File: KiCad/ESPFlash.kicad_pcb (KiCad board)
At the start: 2 copper layers, 29.8 x 23 mm, 26 parts, among them J1 USB-C-16P (USB 2.0 only), J2 ESPFlash, Q1 MMDT3904, U1 TLV75533PDBVR, U2 USBLC6-4SC6, U3 CP2102N-Axx-xQFN24

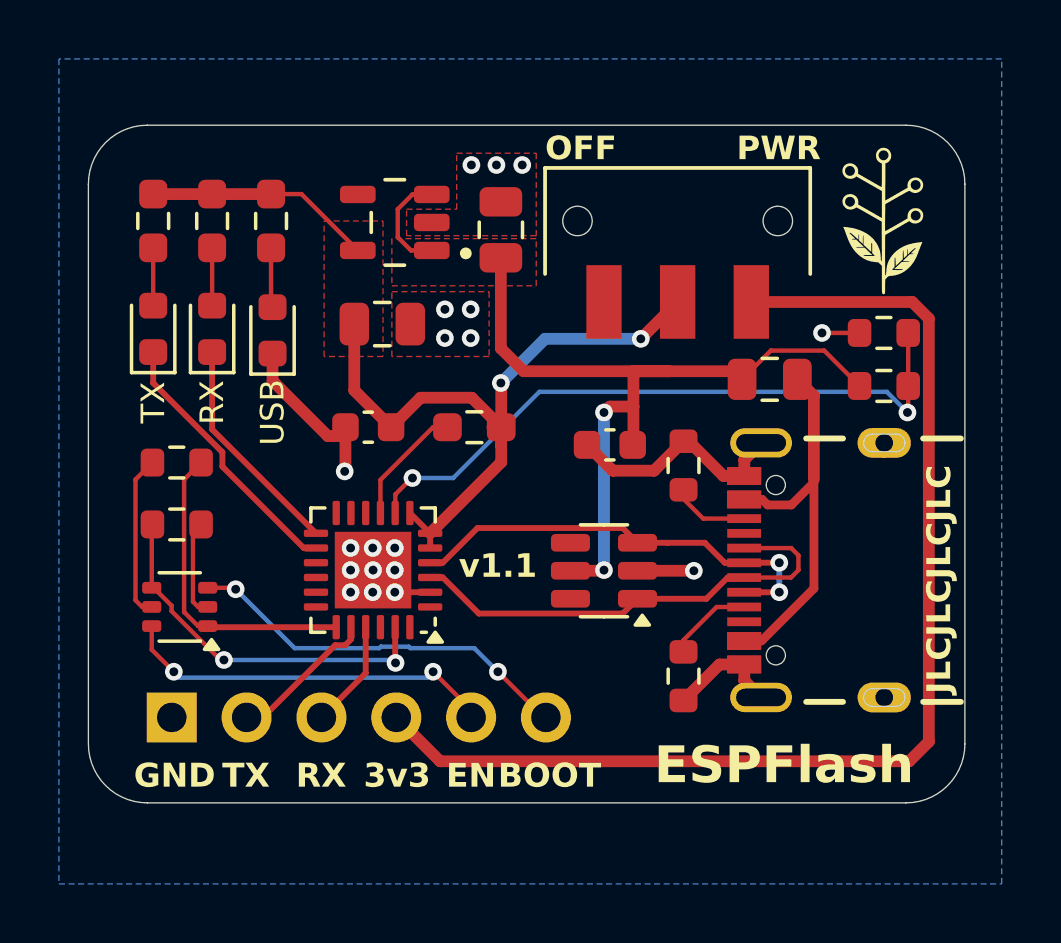
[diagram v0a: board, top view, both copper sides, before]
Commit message: Update BoM
Update components with full description and Digikey P/N.
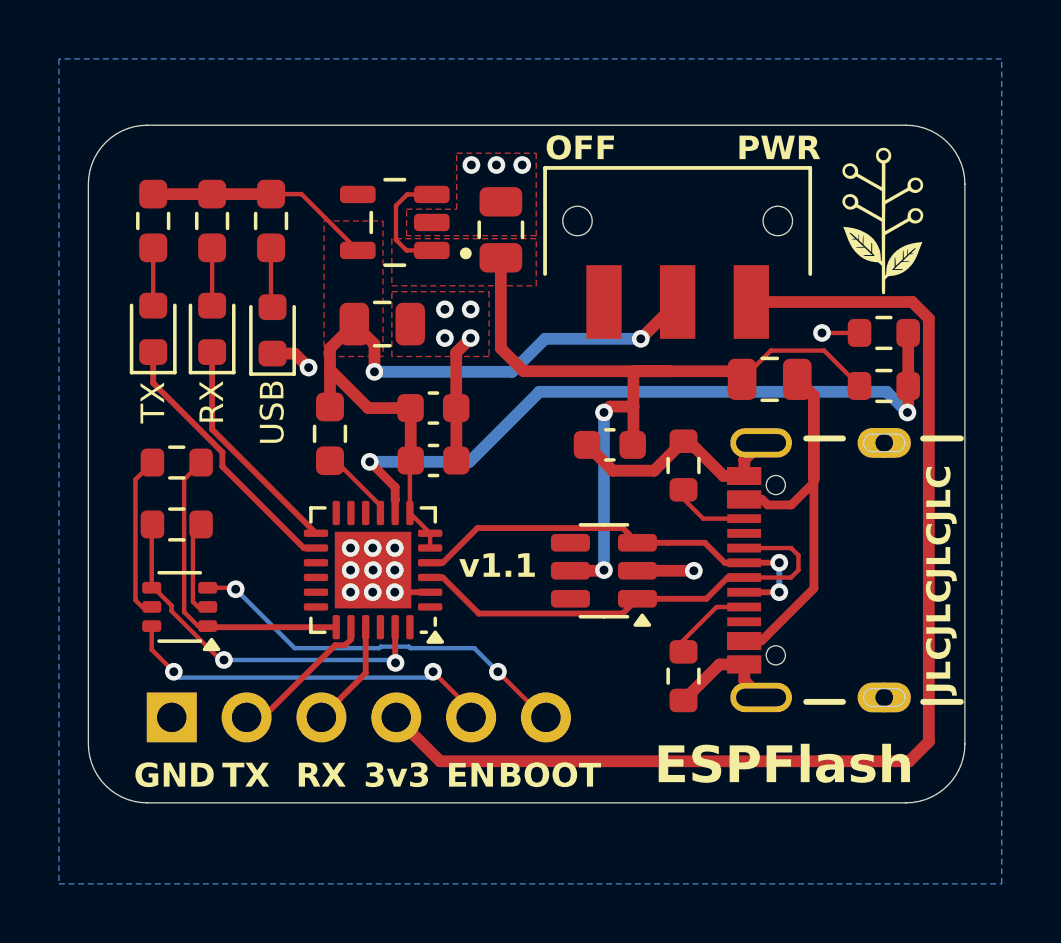
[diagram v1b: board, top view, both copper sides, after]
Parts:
- added C4: 4.7u, Capacitor_SMD:C_0603_1608Metric, F.Cu at (48.7, 30.9)
- moved R4 4.91 mm to (45.2, 31.7), turned to 90 degrees
- moved C5 2.49 mm to (48.7, 32.6), turned to 0 degrees
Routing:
- net Net-(U3-~{RST}): track 4.14 -> 2.60 mm
- net Net-(U3-VBUS): track 22.4 -> 23.9 mm
- net +3.3V: track 31.4 -> 32.6 mm
- net GND: track 21.8 -> 22.6 mm

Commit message: Update BOM and general tidy-up
Include DigiKey cut-tape components and add flag to indicate own stocked items. Remove files that aren't part of the sharable project (KiCad 9 embeds), Remove empty/irrelevant folders.
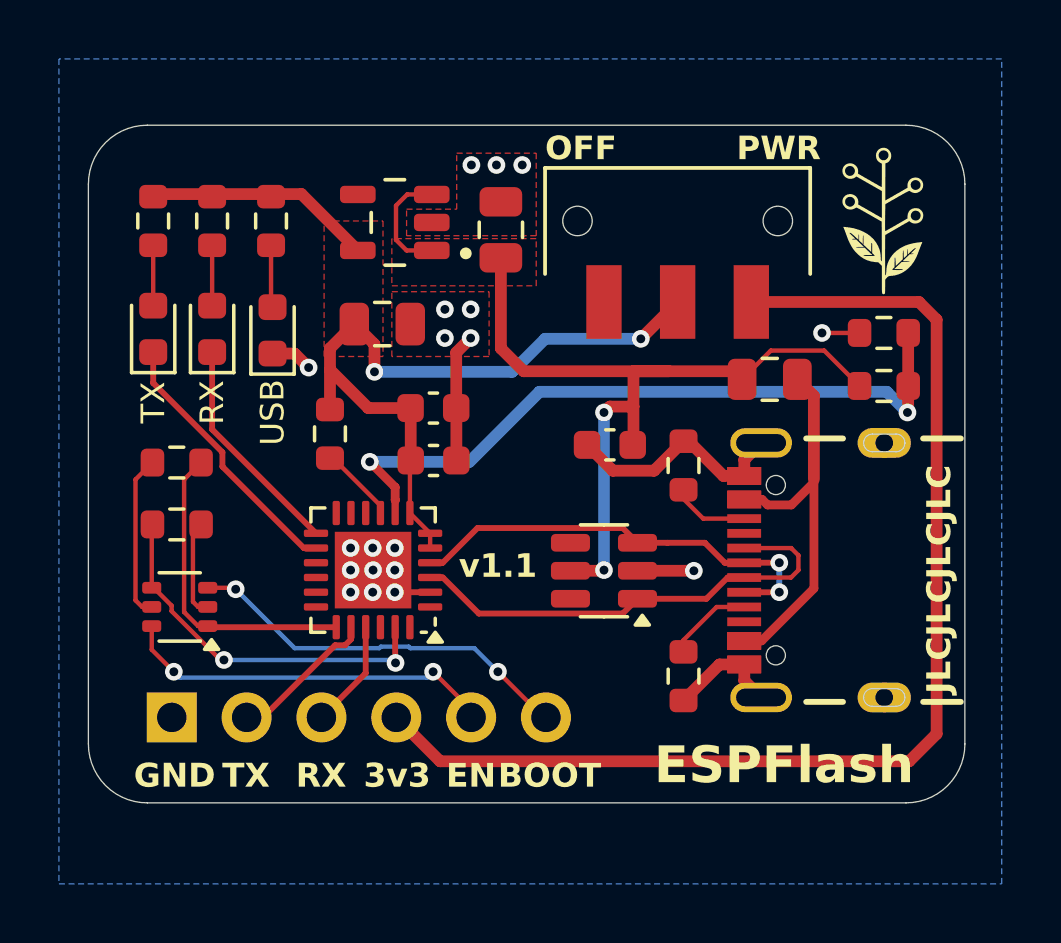
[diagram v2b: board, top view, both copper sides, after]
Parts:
- R1, R4, R5, R6: footprint Resistor_SMD:R_0603_1608Metric_Pad0.98x0.95mm_HandSolder -> Resistor_SMD:R_0603_1608Metric
- R7, R8: value 10K -> 10k
